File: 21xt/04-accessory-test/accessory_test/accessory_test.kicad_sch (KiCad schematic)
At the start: 10 parts, among them J1 Conn_01x44, J2 Conn_01x01, J3 Conn_01x02, U3 Teensy4.1

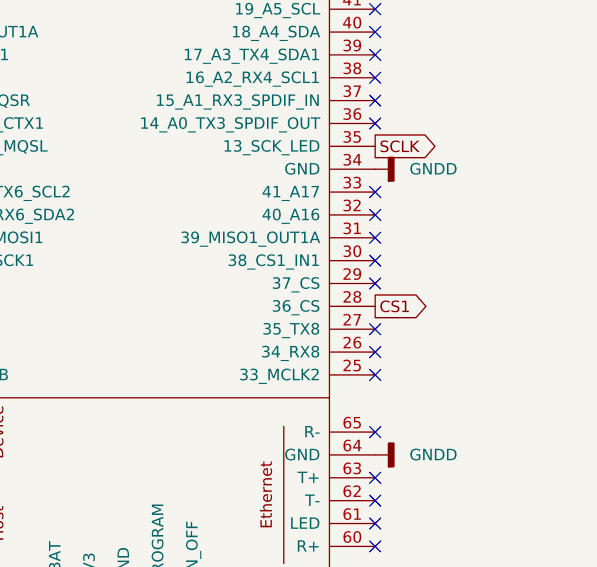
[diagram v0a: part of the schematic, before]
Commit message: rough draft of max5719 breakout board
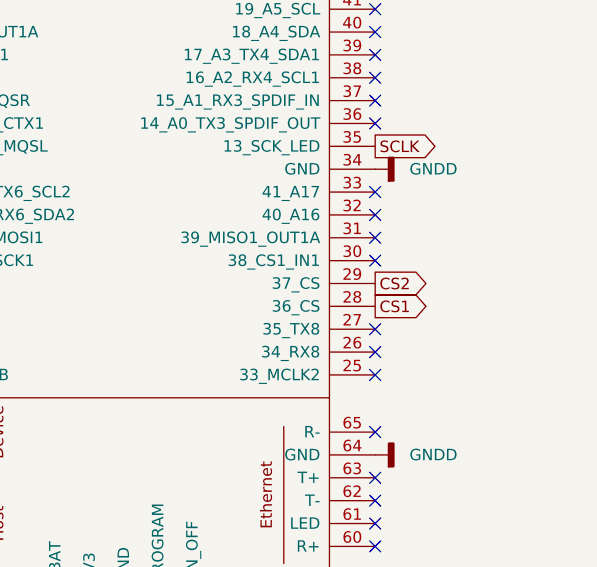
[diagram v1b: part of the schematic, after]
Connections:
- net CS2: now reaches U3.29 (37_CS)
- no-connect marks 56 -> 55
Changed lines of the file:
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@@
-	)
-	(no_connect
-		(at 251.46 93.98)
 	)
 	(no_connect
@@
 		)
 	)
+	(global_label "CS1"
+		(shape output)
+		(at 251.46 96.52 0)
+		(fields_autoplaced yes)
+		(effects
+			(font
+				(size 1.27 1.27)
+			)
+			(justify left)
+		)
+		(property "Intersheetrefs" "${INTERSHEET_REFS}"
+			(at 258.1342 96.52 0)
+			(effects
+				(font
+					(size 1.27 1.27)
+				)
+				(justify left)
+				(hide yes)
+			)
+		)
+	)
 	(global_label "DOUT4"
 		(shape input)
@@
 		)
 	)
-	(global_label "CS1"
-		(shape output)
-		(at 251.46 96.52 0)
-		(fields_autoplaced yes)
-		(effects
-			(font
-				(size 1.27 1.27)
-			)
-			(justify left)
-		)
-		(property "Intersheetrefs" "${INTERSHEET_REFS}"
-			(at 258.1342 96.52 0)
-			(effects
-				(font
-					(size 1.27 1.27)
-				)
-				(justify left)
-				(hide yes)
-			)
-		)
-	)
 	(global_label "CS"
 		(shape output)
@@
 				(hide yes)
 			)
+		)
+	)
+	(global_label "CS2"
+		(shape output)
+		(at 251.46 93.98 0)
+		(fields_autoplaced yes)
+		(effects
+			(font
+				(size 1.27 1.27)
+			)
+			(justify left)
+		)
+		(property "Intersheetrefs" "${INTERSHEET_REFS}"
+			(at 258.1342 93.98 0)
+			(effects
+				(font
+					(size 1.27 1.27)
+				)
+				(justify left)
+				(hide yes)
+			)

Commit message: finish max5719 breakout board
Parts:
- U3: footprint accessory_test:teensy4.1 -> accessory_test:Teensy41
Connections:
- net DIN0: now also U3.11 (9_OUT1C); no longer U3.6 (4_BCLK2)
- net DIN1: now also U3.10 (8_TX2_IN1); no longer U3.7 (5_IN2)
- net DIN2: now also U3.9 (7_RX2_OUT1A); no longer U3.8 (6_OUT1D)
- net DIN3: now also U3.8 (6_OUT1D); no longer U3.9 (7_RX2_OUT1A)
- net DIN4: now also U3.7 (5_IN2); no longer U3.10 (8_TX2_IN1)
- net DIN5: now also U3.6 (4_BCLK2); no longer U3.11 (9_OUT1C)
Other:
- added sheet strain_resistor_array (strain_resistor_array.kicad_sch)
- moved on the sheet: J2

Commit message: finish max5719 breakout board
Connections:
- net S6: now reaches U3.40 (18_A4_SDA)
- net S5: now reaches U3.41 (19_A5_SCL)
- net S4: now reaches U3.42 (20_A6_TX5_LRCLK1)
- net S3: now reaches U3.43 (21_A7_RX5_BCLK1)
- net S2: now reaches U3.44 (22_A8_CTX1)
- net S1: now reaches U3.45 (23_A9_CRX1_MCLK1)
- no-connect marks 55 -> 49
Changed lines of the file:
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@@
-	)
-	(no_connect
-		(at 251.46 63.5)
-	)
-	(no_connect
-		(at 251.46 58.42)
 	)
 	(no_connect
@@
 	)
 	(no_connect
-		(at 251.46 66.04)
-	)
-	(no_connect
 		(at 25.4 91.44)
 	)
@@
 	)
 	(no_connect
-		(at 251.46 55.88)
-	)
-	(no_connect
 		(at 219.71 133.35)
 	)
@@
 	)
 	(no_connect
-		(at 251.46 60.96)
-	)
-	(no_connect
 		(at 251.46 88.9)
 	)
@@
 	(no_connect
 		(at 251.46 50.8)
-	)
-	(no_connect
-		(at 251.46 53.34)
 	)
 	(no_connect
@@
 		)
 	)
+	(global_label "S2"
+		(shape input)
+		(at 251.46 55.88 0)
+		(fields_autoplaced yes)
+		(effects
+			(font
+				(size 1.27 1.27)
+			)
+			(justify left)
+		)
+		(property "Intersheetrefs" "${INTERSHEET_REFS}"
+			(at 256.8642 55.88 0)
+			(effects
+				(font
+					(size 1.27 1.27)
+				)
+				(justify left)
+				(hide yes)
+			)
+		)
+	)
+	(global_label "S3"
+		(shape input)
+		(at 251.46 58.42 0)
+		(fields_autoplaced yes)
+		(effects
+			(font
+				(size 1.27 1.27)
+			)
+			(justify left)
+		)
+		(property "Intersheetrefs" "${INTERSHEET_REFS}"
+			(at 256.8642 58.42 0)
+			(effects
+				(font
+					(size 1.27 1.27)
+				)
+				(justify left)
+				(hide yes)
+			)
+		)
+	)
 	(global_label "DOUT1"
 		(shape input)
@@
 		)
 	)
+	(global_label "S4"
+		(shape input)
+		(at 251.46 60.96 0)
+		(fields_autoplaced yes)
+		(effects
+			(font
+				(size 1.27 1.27)
+			)
+			(justify left)
+		)
+		(property "Intersheetrefs" "${INTERSHEET_REFS}"
+			(at 256.8642 60.96 0)
+			(effects
+				(font
+					(size 1.27 1.27)
+				)
+				(justify left)
+				(hide yes)
+			)
+		)
+	)
 	(global_label "SCLK"
 		(shape output)
@@
 		)
 	)
+	(global_label "S1"
+		(shape input)
+		(at 251.46 53.34 0)
+		(fields_autoplaced yes)
+		(effects
+			(font
+				(size 1.27 1.27)
+			)
+			(justify left)
+		)
+		(property "Intersheetrefs" "${INTERSHEET_REFS}"
+			(at 256.8642 53.34 0)
+			(effects
+				(font
+					(size 1.27 1.27)
+				)
+				(justify left)
+				(hide yes)
+			)
+		)
+	)
 	(global_label "DOUT3"
 		(shape input)
@@
 		)
 	)
+	(global_label "S6"
+		(shape input)
+		(at 251.46 66.04 0)
+		(fields_autoplaced yes)
+		(effects
+			(font
+				(size 1.27 1.27)
+			)
+			(justify left)
+		)
+		(property "Intersheetrefs" "${INTERSHEET_REFS}"
+			(at 256.8642 66.04 0)
+			(effects
+				(font
+					(size 1.27 1.27)
+				)
+				(justify left)
+				(hide yes)
+			)
+		)
+	)
 	(global_label "DIN0"
 		(shape output)
@@
 			(effects
 				(font
+					(size 1.27 1.27)
+				)
+				(justify left)
+				(hide yes)
+			)
+		)
+	)
+	(global_label "S5"
+		(shape input)
+		(at 251.46 63.5 0)
+		(fields_autoplaced yes)
+		(effects
+			(font
+				(size 1.27 1.27)
+			)
+			(justify left)
+		)
+		(property "Intersheetrefs" "${INTERSHEET_REFS}"
+			(at 256.8642 63.5 0)
+			(effects
+				(font

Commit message: stuff sorry im tired
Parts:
- removed NT1: NetTie_2, NetTie:NetTie-2_THT_Pad1.0mm, symbol Device:NetTie_2
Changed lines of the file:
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@@
-	)
-	(symbol
-		(lib_id "Device:NetTie_2")
-		(at 58.42 74.93 0)
-		(unit 1)
-		(exclude_from_sim no)
-		(in_bom no)
-		(on_board yes)
-		(dnp no)
-		(fields_autoplaced yes)
-		(property "Reference" "NT1"
-			(at 58.42 69.85 0)
-			(effects
-				(font
-					(size 1.27 1.27)
-				)
-			)
-		)
-		(property "Value" "NetTie_2"
-			(at 58.42 72.39 0)
-			(effects
-				(font
-					(size 1.27 1.27)
-				)
-			)
-		)
-		(property "Footprint" "NetTie:NetTie-2_THT_Pad1.0mm"
-			(at 58.42 74.93 0)
-			(effects
-				(font
-					(size 1.27 1.27)
-				)
-				(hide yes)
-			)
-		)
-		(property "Datasheet" "~"
-			(at 58.42 74.93 0)
-			(effects
-				(font
-					(size 1.27 1.27)
-				)
-				(hide yes)
-			)
-		)
-		(property "Description" ""
-			(at 58.42 74.93 0)
-			(effects
-				(font
-					(size 1.27 1.27)
-				)
-				(hide yes)
-			)
-		)
-		(pin "1"
-		)
-		(pin "2"
-		)
-		(instances
-			(project "accessory_test"
-				(path "/ff30e7ea-42b3-4dfc-9081-b802076eea15"
-					(reference "NT1")
-					(unit 1)
-				)
-			)
-		)
 	)
 	(symbol
@@
 	(symbol
 		(lib_id "power:GNDD")
-		(at 60.96 74.93 90)
+		(at 67.31 76.2 90)
 		(unit 1)
 		(exclude_from_sim no)
@@
 		(fields_autoplaced yes)
 		(property "Reference" "#PWR01"
-			(at 67.31 74.93 0)
+			(at 73.66 76.2 0)
 			(effects
 				(font
@@
 		)
 		(property "Value" "GNDD"
-			(at 64.77 74.93 90)
+			(at 71.12 76.2 90)
 			(effects
 				(font
@@
 		)
 		(property "Footprint" ""
-			(at 60.96 74.93 0)
+			(at 67.31 76.2 0)
 			(effects
 				(font
@@
 		)
 		(property "Datasheet" ""
-			(at 60.96 74.93 0)
+			(at 67.31 76.2 0)
 			(effects
 				(font
@@
 		)
 		(property "Description" ""
-			(at 60.96 74.93 0)
-			(effects
-				(font
+			(at 67.31 76.2 0)
+			(effects
+				(font

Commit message: layout progress on test board
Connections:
- net DIN1: now also U3.9 (7_RX2_OUT1A); no longer U3.10 (8_TX2_IN1)
- net DIN2: now also U3.7 (5_IN2); no longer U3.9 (7_RX2_OUT1A)
- net DIN3: now also U3.10 (8_TX2_IN1); no longer U3.8 (6_OUT1D)
- net DIN4: now also U3.8 (6_OUT1D); no longer U3.7 (5_IN2)
- net S5: now also U3.40 (18_A4_SDA); no longer U3.41 (19_A5_SCL)
- net S6: now also U3.41 (19_A5_SCL); no longer U3.40 (18_A4_SDA)

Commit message: finished up layout
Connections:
- net GNDD is gone; now on net GNDA: D1.2 (A), J2.1 (Pin_1), J3.1 (Pin_1), U3.1 (GND), U3.34 (GND), U3.47 (GND), U3.52 (GND), U3.58 (GND), U3.59 (GND), U3.64 (GND)
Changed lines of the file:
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@@
+	(wire
+		(pts
+			(xy 60.96 74.93) (xy 55.88 74.93)
+		)
+		(stroke
+			(width 0)
+			(type default)
+		)
+	)
 	(wire
 		(pts
@@
 	(symbol
 		(lib_id "power:GNDD")
-		(at 67.31 76.2 90)
+		(at 60.96 74.93 90)
 		(unit 1)
 		(exclude_from_sim no)
@@
 		(fields_autoplaced yes)
 		(property "Reference" "#PWR01"
-			(at 73.66 76.2 0)
+			(at 67.31 74.93 0)
 			(effects
 				(font
@@
 		)
 		(property "Value" "GNDD"
-			(at 71.12 76.2 90)
+			(at 64.77 74.93 90)
 			(effects
 				(font
@@
 		)
 		(property "Footprint" ""
-			(at 67.31 76.2 0)
+			(at 60.96 74.93 0)
 			(effects
 				(font
@@
 		)
 		(property "Datasheet" ""
-			(at 67.31 76.2 0)
+			(at 60.96 74.93 0)
 			(effects
 				(font
@@
 		)
 		(property "Description" ""
-			(at 67.31 76.2 0)
-			(effects
-				(font
+			(at 60.96 74.93 0)
+			(effects
+				(font

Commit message: v2 layout initial commit
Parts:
- removed J1: Conn_01x44, Connector_Dsub:DSUB-44-HD_Male_Horizontal_P2.29x2.54mm_EdgePinOffset9.40mm, symbol Connector_Generic:Conn_01x44
- added J4: DB44, accessory_test:DB44, symbol accessory_test:DB44
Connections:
- net 12v: now also J4.23, J4.8
- net 5BUCK: now also J4.35, J4.36
- net 5VAR: now also J4.39, J4.40
- net AOUT0: now also J4.28
- net AOUT1: now also J4.9
- net AOUT2: now also J4.10
- net AOUT3: now also J4.11
- net AOUT4: now also J4.12
- net AOUT5: now also J4.13
- net AOUT6: now also J4.24
- net AOUT7: now also J4.25
- net AOUT8: now also J4.26
- net AOUT9: now also J4.27
- net DOUT0: now also J4.7
- net DOUT1: now also J4.6
- net DOUT2: now also J4.5
- net DOUT3: now also J4.22
- net DOUT4: now also J4.21
- net DOUT5: now also J4.20
- net GNDA: now also J4.33, J4.34, J4.37, J4.41, J4.42
- net QS1+: now also J4.43
- net QS2+: now also J4.44
- net RX: now reaches U3.2 (0_RX1_CRX2_CS1)
- net TX: now reaches U3.3 (1_TX1_CTX2_MISO1)
- net 3v3 renamed 3V3
- net 3V3: now also J4.31, J4.32
- new net QS1F-: J4.29
- new net QS1S-: J4.14
- new net QS2F-: J4.30
- new net QS2S-: J4.15
- no-connect marks 49 -> 44

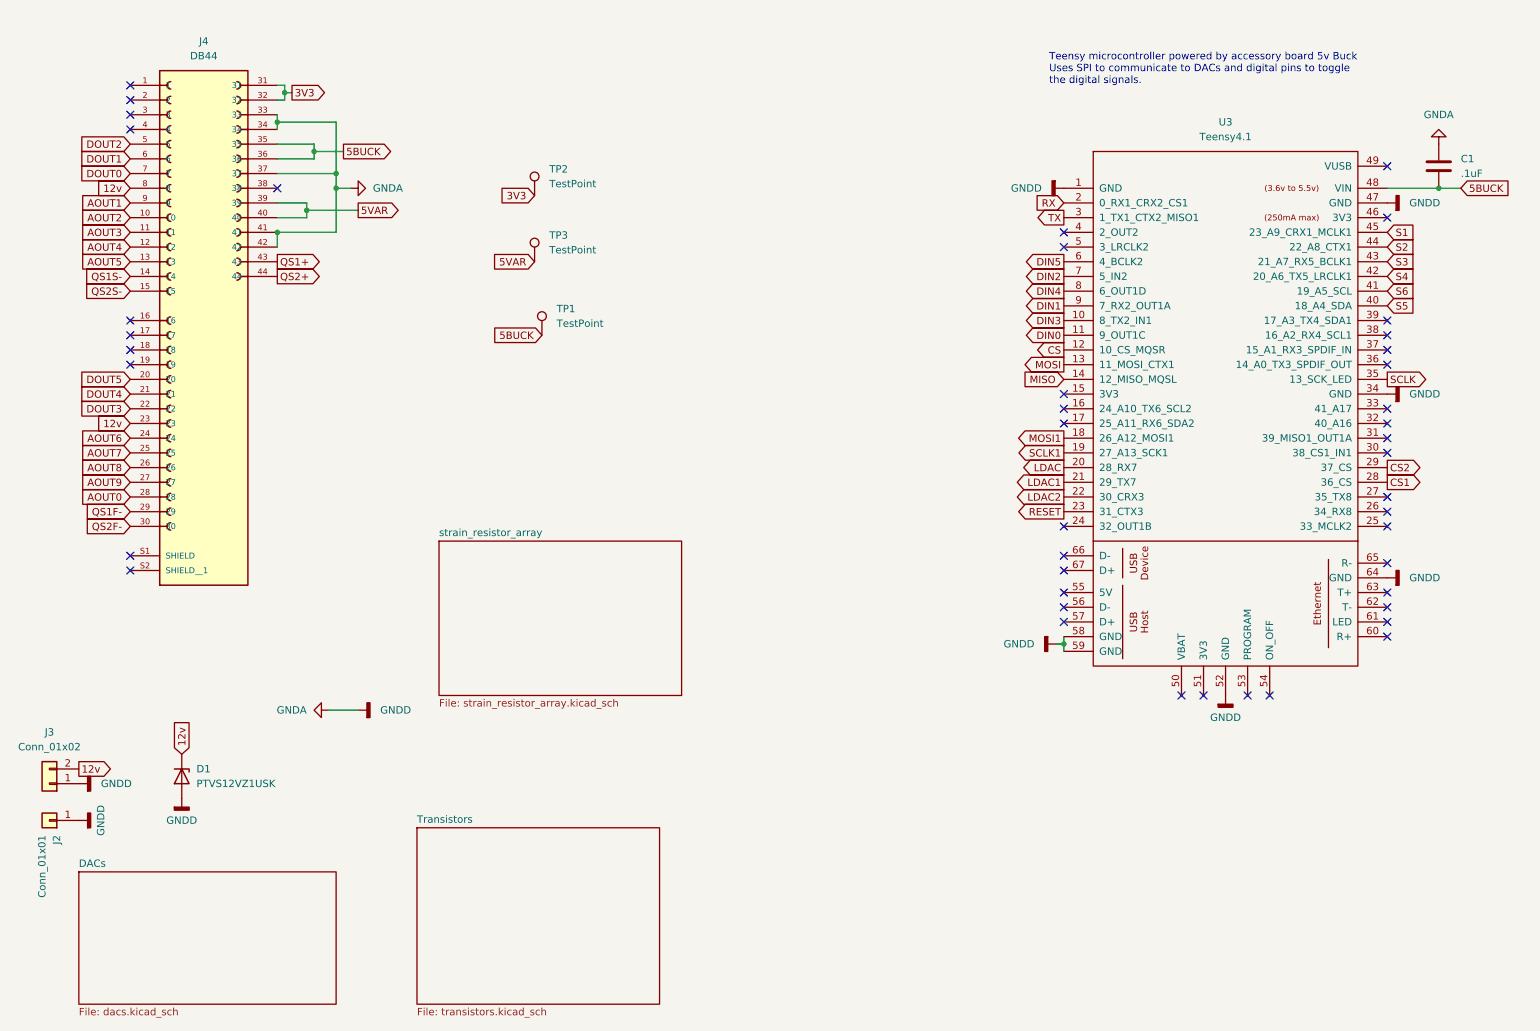
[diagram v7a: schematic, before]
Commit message: add um3208uk for spi and uart
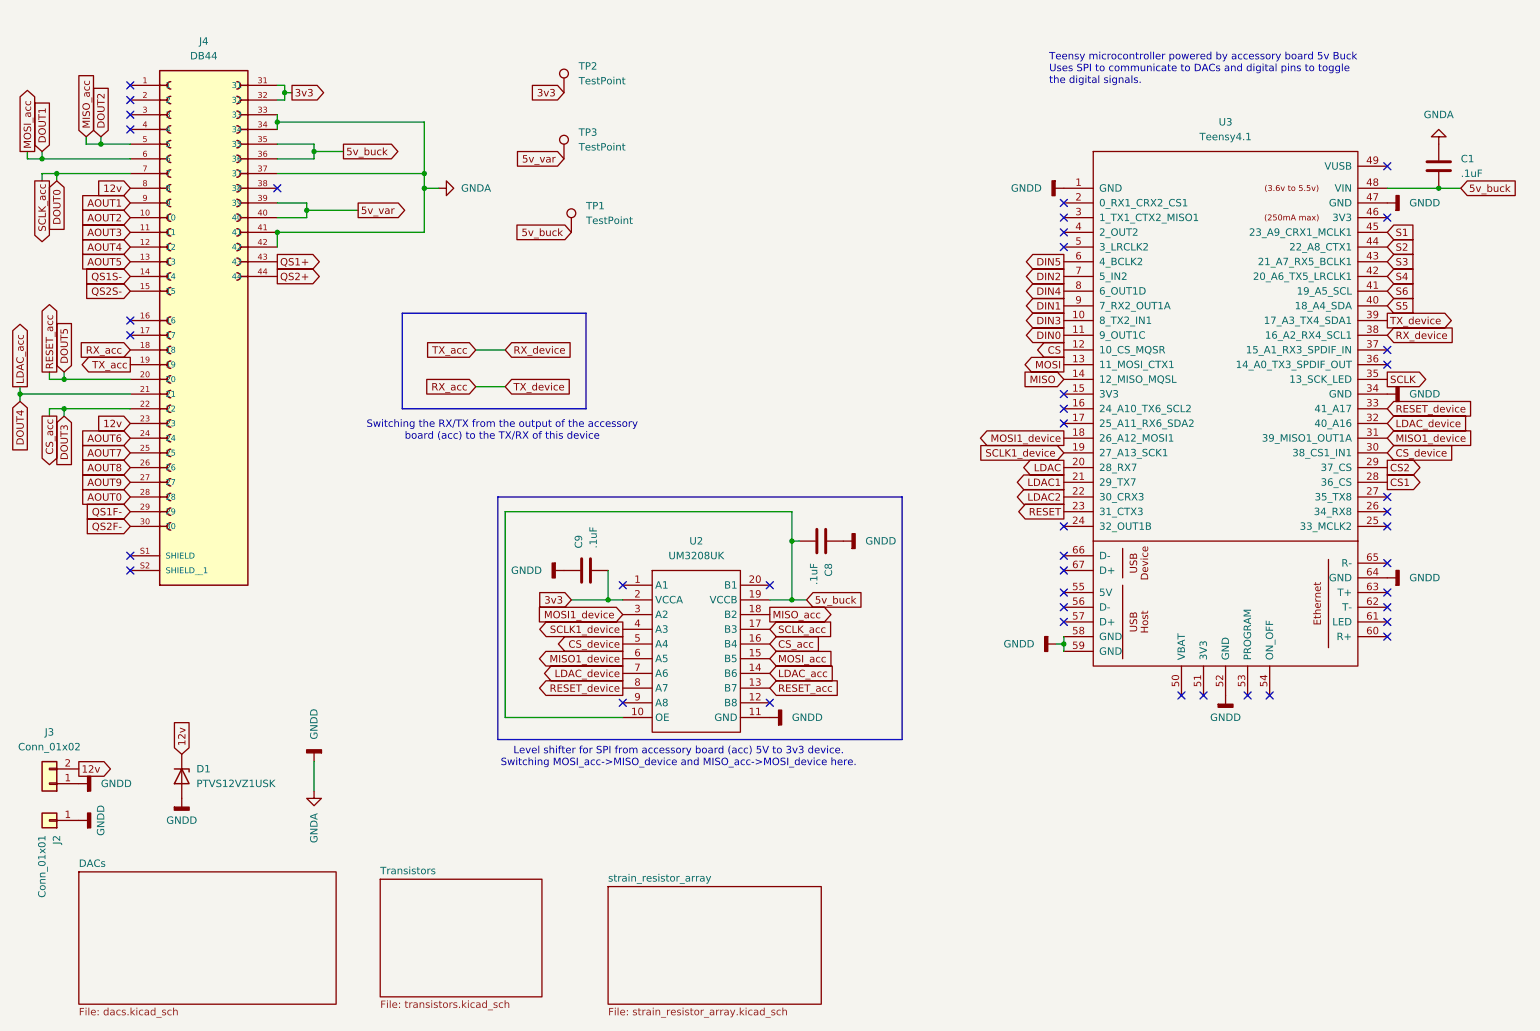
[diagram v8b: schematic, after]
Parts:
- added C8, C9: .1uF, Capacitor_SMD:C_0603_1608Metric, symbol Device:C
- added U2: UM3208UK, Package_SO:TSSOP-20_4.4x6.5mm_P0.65mm, symbol accessory_test:UM3208UK
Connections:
- net DOUT0: now also U2.17 (B3)
- net DOUT1: now also U2.15 (B5)
- net DOUT2: now also U2.18 (B2)
- net DOUT4: now also U2.14 (B6)
- net DOUT5: now also U2.13 (B7)
- net GNDA: now also C8.1, C9.1, U2.11 (GND)
- net RX_acc: now reaches J4.18
- net RX_acc: now also U3.39 (17_A3_TX4_SDA1)
- net RX_device: now reaches J4.19
- net RX_device: now also U3.38 (16_A2_RX4_SCL1)
- net CS_device: now reaches U3.30 (38_CS1_IN1)
- net CS_device: now also U2.5 (A4)
- net MISO1_device: now reaches U3.31 (39_MISO1_OUT1A)
- net MISO1_device: now also U2.6 (A5)
- net LDAC_device: now reaches U3.32 (40_A16)
- net LDAC_device: now also U2.7 (A6)
- net RESET_device: now reaches U3.33 (41_A17)
- net RESET_device: now also U2.8 (A7)
- net 3V3 renamed 3v3
- net 3v3: now also C9.2, U2.2 (VCCA)
- net 5BUCK renamed 5v_buck
- net 5v_buck: now also C8.2, U2.10 (OE), U2.19 (VCCB)
- net 5VAR renamed 5v_var
- net DOUT3 renamed CS_acc
- net CS_acc: now also U2.16 (B4)
- net MOSI1 renamed MOSI1_device
- net MOSI1_device: now also U2.3 (A2)
- net RX: no longer names the net of U3.2 (0_RX1_CRX2_CS1)
- net SCLK1 renamed SCLK1_device
- net SCLK1_device: now also U2.4 (A3)
- net TX: no longer names the net of U3.3 (1_TX1_CTX2_MISO1)
- no-connect marks 44 -> 42
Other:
- note added: "Level shifter for SPI from accessory board (acc) 5V to 3v3 device. Switching MOSI_acc->MISO_device and MISO_acc->MOSI_device here."
- note added: "Switching the RX/TX from the output of the accessory board (acc) to the TX/RX of this device"
- moved on the sheet: TP1, TP2, TP3
